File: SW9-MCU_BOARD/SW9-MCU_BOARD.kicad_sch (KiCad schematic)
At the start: 20 parts, among them IC1 STM32L051C6T6, J1 Conn_ARM_JTAG_SWD_10, SW1 SW_DPDT_x2, SW2 SW_Push_Dual, Y1 32KHz, Y2 8MHz

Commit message: schematic cleanup
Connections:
- net VDD: now also J1.1 (VTref)
- net SWDIO/TMS: now reaches IC1.34 (PA13)
- net SWDIO/TMS: now also J1.2 (SWDIO/TMS)
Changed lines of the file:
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@@
     (stroke (width 0) (type default))
   )
-  (wire (pts (xy 78.74 104.14) (xy 78.74 73.66))
+  (wire (pts (xy 71.12 73.66) (xy 71.12 114.3))
     (stroke (width 0) (type default))
   )
@@
     (stroke (width 0) (type default))
   )
-  (wire (pts (xy 175.26 71.12) (xy 184.15 71.12))
+  (wire (pts (xy 182.88 67.31) (xy 189.23 67.31))
     (stroke (width 0) (type default))
   )
@@
     (stroke (width 0) (type default))
   )
+  (wire (pts (xy 175.26 73.66) (xy 181.61 73.66))
+    (stroke (width 0) (type default))
+  )
   (wire (pts (xy 224.79 135.89) (xy 240.03 135.89))
     (stroke (width 0) (type default))
@@
     (stroke (width 0) (type default))
   )
+  (wire (pts (xy 182.88 67.31) (xy 182.88 71.12))
+    (stroke (width 0) (type default))
+  )
   (wire (pts (xy 157.48 40.64) (xy 158.75 40.64))
     (stroke (width 0) (type default))
@@
     (stroke (width 0) (type default))
   )
+  (wire (pts (xy 182.88 71.12) (xy 175.26 71.12))
+    (stroke (width 0) (type default))
+  )
   (wire (pts (xy 132.08 142.24) (xy 143.51 142.24))
     (stroke (width 0) (type default))
@@
     (stroke (width 0) (type default))
   )
-  (wire (pts (xy 96.52 76.2) (xy 132.08 76.2))
+  (wire (pts (xy 87.63 76.2) (xy 132.08 76.2))
     (stroke (width 0) (type default))
   )
@@
     (stroke (width 0) (type default))
   )
-  (wire (pts (xy 96.52 106.68) (xy 96.52 76.2))
-    (stroke (width 0) (type default))
-  )
   (wire (pts (xy 87.63 116.84) (xy 87.63 114.3))
     (stroke (width 0) (type default))
@@
     (stroke (width 0) (type default))
   )
-  (wire (pts (xy 71.12 104.14) (xy 78.74 104.14))
-    (stroke (width 0) (type default))
-  )
   (wire (pts (xy 157.48 142.24) (xy 157.48 147.32))
     (stroke (width 0) (type default))
@@
     (stroke (width 0) (type default))
   )
-  (wire (pts (xy 121.92 68.58) (xy 121.92 88.9))
-    (stroke (width 0) (type default))
-  )
   (wire (pts (xy 198.12 128.27) (xy 198.12 125.73))
     (stroke (width 0) (type default))
@@
     (stroke (width 0) (type default))
   )
+  (wire (pts (xy 92.71 151.13) (xy 101.6 151.13))
+    (stroke (width 0) (type default))
+  )
   (wire (pts (xy 132.08 143.51) (xy 132.08 142.24))
     (stroke (width 0) (type default))
@@
     (stroke (width 0) (type default))
   )
-  (wire (pts (xy 87.63 106.68) (xy 96.52 106.68))
-    (stroke (width 0) (type default))
-  )
   (wire (pts (xy 144.78 41.91) (xy 144.78 43.18))
     (stroke (width 0) (type default))
@@
     (stroke (width 0) (type default))
   )
-  (wire (pts (xy 78.74 73.66) (xy 132.08 73.66))
+  (wire (pts (xy 71.12 73.66) (xy 132.08 73.66))
     (stroke (width 0) (type default))
   )
@@
     (stroke (width 0) (type default))
   )
-  (wire (pts (xy 87.63 114.3) (xy 87.63 106.68))
+  (wire (pts (xy 87.63 76.2) (xy 87.63 114.3))
     (stroke (width 0) (type default))
   )
@@
     (stroke (width 0) (type default))
   )
-  (wire (pts (xy 71.12 114.3) (xy 71.12 104.14))
-    (stroke (width 0) (type default))
-  )
   (wire (pts (xy 165.1 120.65) (xy 165.1 114.3))
     (stroke (width 0) (type default))
   )
-  (wire (pts (xy 121.92 88.9) (xy 132.08 88.9))
+  (wire (pts (xy 125.73 88.9) (xy 132.08 88.9))
     (stroke (width 0) (type default))
   )
   (wire (pts (xy 129.54 68.58) (xy 132.08 68.58))
     (stroke (width 0) (type default))
+  )
+  (global_label "SWDIO{slash}TMS" (shape input) (at 181.61 73.66 0) (fields_autoplaced)
+    (effects (font (size 1.27 1.27)) (justify left))
+    (property "Intersheetrefs" "${INTERSHEET_REFS}" (at 195.4204 73.66 0)
+      (effects (font (size 1.27 1.27)) (justify left) hide)
+    )
+  )
+  (global_label "SWDIO{slash}TMS" (shape output) (at 101.6 151.13 0) (fields_autoplaced)
+    (effects (font (size 1.27 1.27)) (justify left))
+    (property "Intersheetrefs" "${INTERSHEET_REFS}" (at 115.4104 151.13 0)
+      (effects (font (size 1.27 1.27)) (justify left) hide)
+    )
   )
   (symbol (lib_id "Switch:SW_DPDT_x2") (at 163.83 40.64 0) (unit 1)
@@
     )
   )
-  (symbol (lib_id "power:VDDA") (at 121.92 68.58 0) (unit 1)
-    (in_bom yes) (on_board yes) (dnp no) (fields_autoplaced)
-    (property "Reference" "#PWR07" (at 121.92 72.39 0)
-      (effects (font (size 1.27 1.27)) hide)
-    )
-    (property "Value" "VDDA" (at 121.92 63.5 0)
-      (effects (font (size 1.27 1.27)))
-    )
-    (property "Footprint" "" (at 121.92 68.58 0)
-      (effects (font (size 1.27 1.27)) hide)
-    )
-    (property "Datasheet" "" (at 121.92 68.58 0)
+  (symbol (lib_id "power:VDDA") (at 125.73 88.9 0) (unit 1)
+    (in_bom yes) (on_board yes) (dnp no) (fields_autoplaced)
+    (property "Reference" "#PWR07" (at 125.73 92.71 0)
+      (effects (font (size 1.27 1.27)) hide)
+    )
+    (property "Value" "VDDA" (at 125.73 83.82 0)
+      (effects (font (size 1.27 1.27)))
+    )
+    (property "Footprint" "" (at 125.73 88.9 0)
+      (effects (font (size 1.27 1.27)) hide)
+    )
+    (property "Datasheet" "" (at 125.73 88.9 0)
       (effects (font (size 1.27 1.27)) hide)
     )
@@
     )
   )
-  (symbol (lib_id "power:Earth") (at 184.15 71.12 0) (unit 1)
-    (in_bom yes) (on_board yes) (dnp no) (fields_autoplaced)
-    (property "Reference" "#PWR018" (at 184.15 77.47 0)
-      (effects (font (size 1.27 1.27)) hide)
-    )
-    (property "Value" "Earth" (at 184.15 74.93 0)
-      (effects (font (size 1.27 1.27)) hide)
-    )
-    (property "Footprint" "" (at 184.15 71.12 0)
-      (effects (font (size 1.27 1.27)) hide)
-    )
-    (property "Datasheet" "~" (at 184.15 71.12 0)
+  (symbol (lib_id "power:Earth") (at 189.23 67.31 0) (unit 1)
+    (in_bom yes) (on_board yes) (dnp no) (fields_autoplaced)
+    (property "Reference" "#PWR018" (at 189.23 73.66 0)
+      (effects (font (size 1.27 1.27)) hide)
+    )
+    (property "Value" "Earth" (at 189.23 71.12 0)
+      (effects (font (size 1.27 1.27)) hide)
+    )
+    (property "Footprint" "" (at 189.23 67.31 0)
+      (effects (font (size 1.27 1.27)) hide)
+    )
+    (property "Datasheet" "~" (at 189.23 67.31 0)
       (effects (font (size 1.27 1.27)) hide)
     )
@@
         )
       )
+    )
+  )
+  (symbol (lib_id "power:VDD") (at 80.01 135.89 0) (unit 1)
+    (in_bom yes) (on_board yes) (dnp no) (fields_autoplaced)
+    (property "Reference" "#PWR019" (at 80.01 139.7 0)
+      (effects (font (size 1.27 1.27)) hide)
+    )
+    (property "Value" "VDD" (at 80.01 130.81 0)
+      (effects (font (size 1.27 1.27)))
+    )
+    (property "Footprint" "" (at 80.01 135.89 0)
+      (effects (font (size 1.27 1.27)) hide)
+    )
+    (property "Datasheet" "" (at 80.01 135.89 0)
+      (effects (font (size 1.27 1.27)) hide)
+    )
+    (pin "1")
+    (instances
+      (project "SW9-MCU_BOARD"
+        (path "/98be697d-8cf2-4efe-bafa-8172d9e478e0"
+          (reference "#PWR019") (unit 1)
+        )
+      )

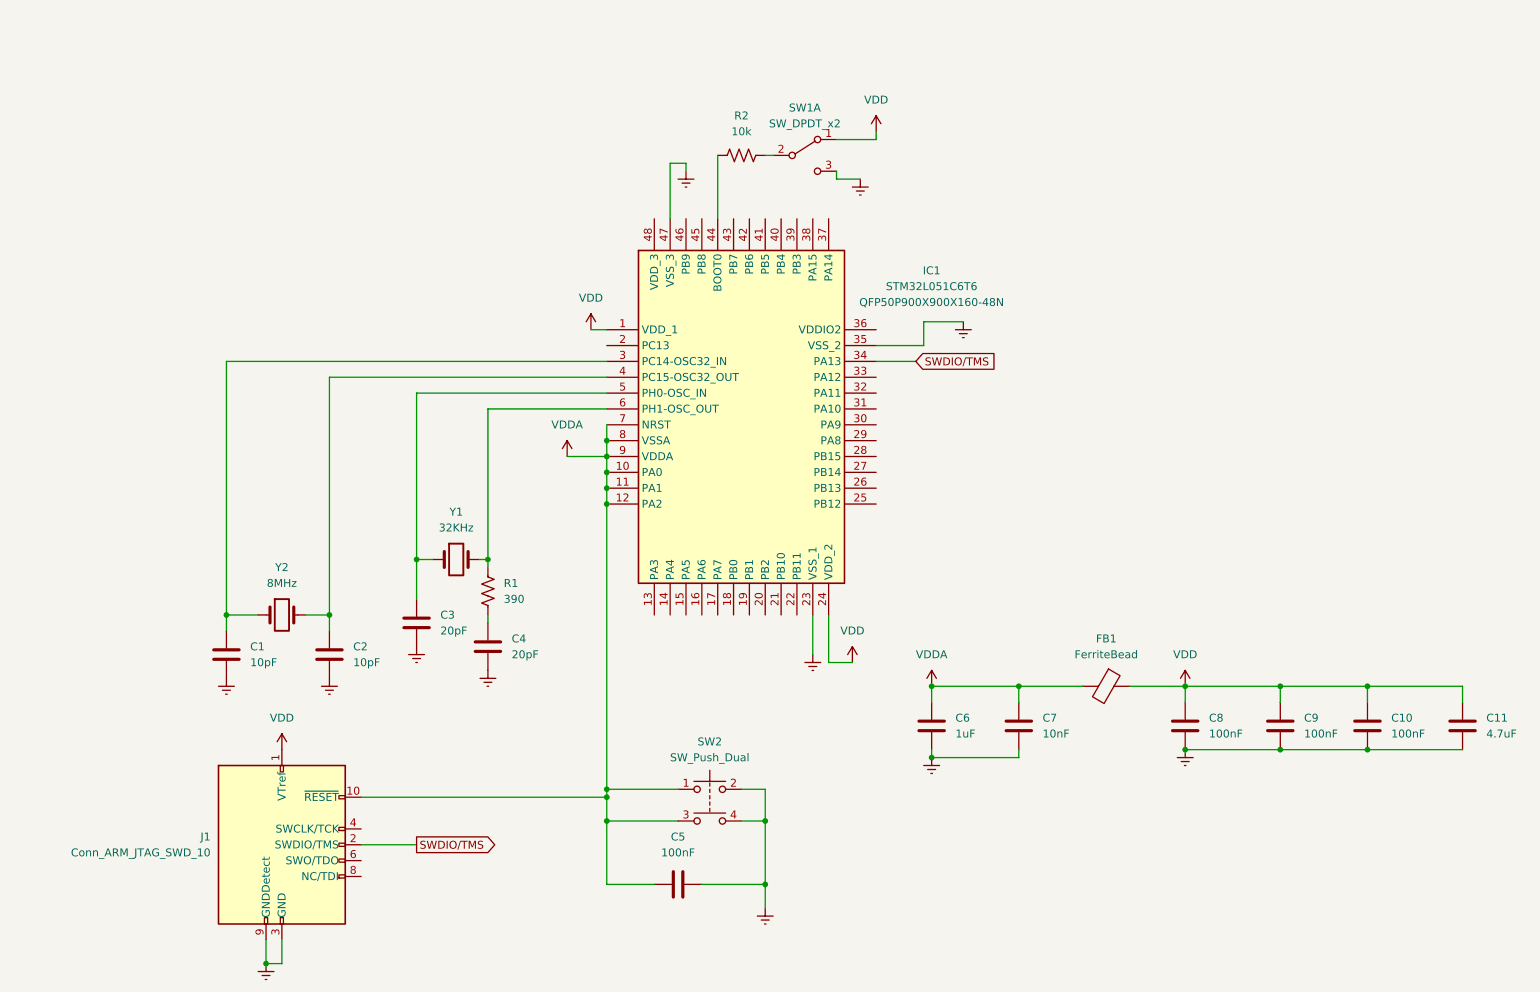
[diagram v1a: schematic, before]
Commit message: more schematic cleanup
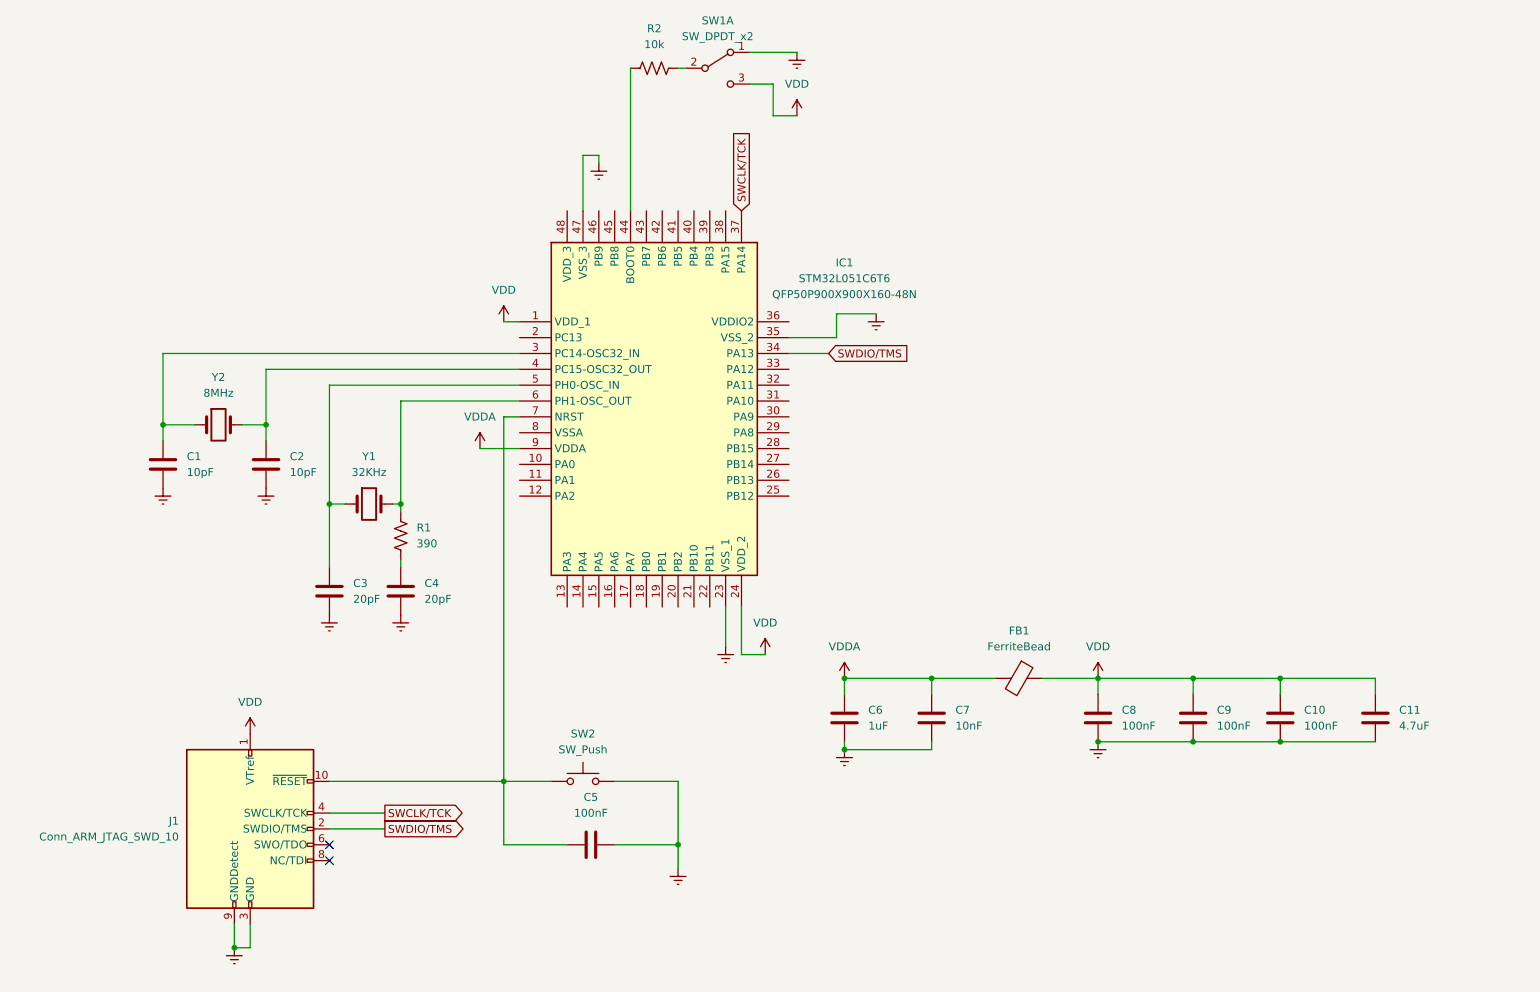
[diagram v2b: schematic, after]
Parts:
- removed SW2: SW_Push_Dual, symbol Switch:SW_Push_Dual
- added SW2: SW_Push, symbol Switch:SW_Push
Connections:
- net Earth: now also SW1.1 (A), SW2.2; no longer SW1.3 (C)
- net VDD: now also SW1.3 (C); no longer SW1.1 (A)
- net VDDA: no longer C5.1, IC1.10 (PA0), IC1.11 (PA1), IC1.12 (PA2), IC1.7 (NRST), IC1.8 (VSSA), J1.10 (~{RESET})
- net SWCLK/TCK: now reaches IC1.37 (PA14)
- net SWCLK/TCK: now also J1.4 (SWCLK/TCK)
- new net: C5.1, IC1.7 (NRST), J1.10 (~{RESET}), SW2.1
- no-connect marks 0 -> 2
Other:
- moved on the sheet: C1, C10, C11, C2, C3, C4, C5, C6, C7, C8, C9, FB1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
